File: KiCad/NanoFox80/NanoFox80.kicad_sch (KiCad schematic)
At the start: 50 parts, among them J101 Conn_01x02, J102 Conn_01x02, J109 Conn_01x02, J111 DB9 Female, J112 Conn_01x02, J113 Conn_01x02, J115 Conn_01x02, P101 ISP/PDI, Q101 BSS84W-7-F, Q102 BSS138W-7-F, SW101 SW_SPST, U102 LP2985-3.3, U105 AVR128DA28, X101 SIT1566AC TCO

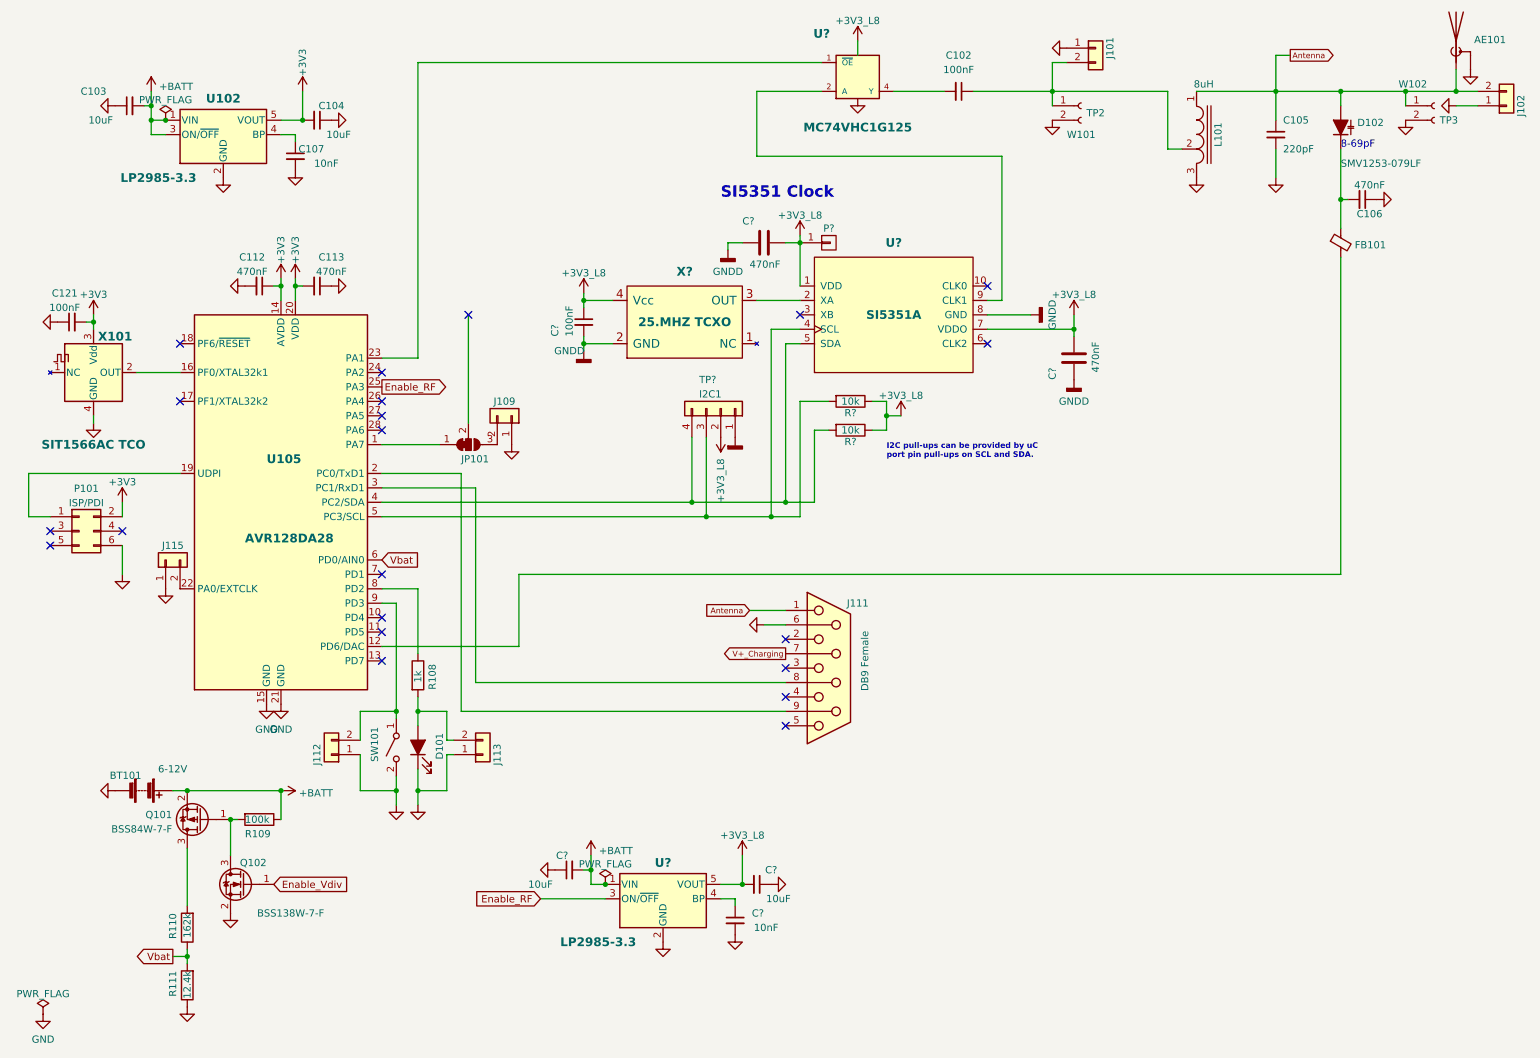
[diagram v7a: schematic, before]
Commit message: Development
o Addressed ERC errors
o Added trimmer capacitor
o Cosmetic changes to schematic
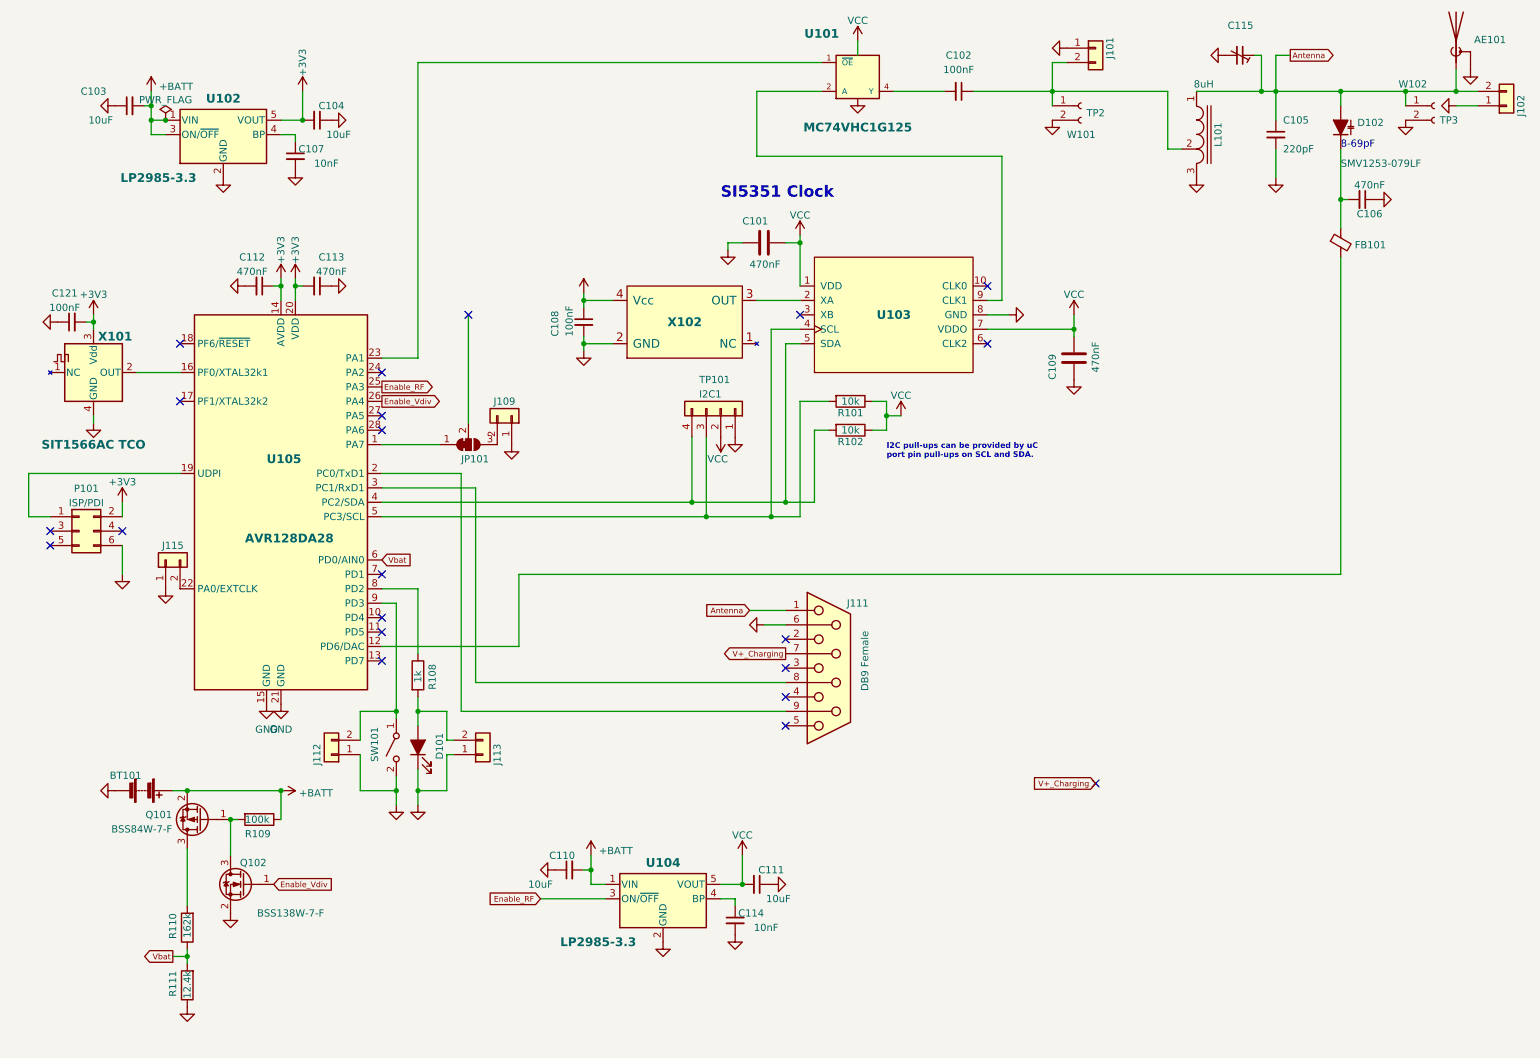
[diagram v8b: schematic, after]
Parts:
- removed P?: Thru, Pin_Headers:Pin_Header_Straight_1x01, symbol FlexFox80-rescue:CONN_01X01-ARDF-2-Band-MiniTx-rescue
- removed U?: SI5351A, Housings_SSOP:MSOP-10_3x3mm_Pitch0.5mm, symbol special:SI5351
- removed X?: 25.MHZ TCXO, Crystals:ASTX-H11-25.000MHZ, symbol special:ASTX-H11
- added C115: (no value), symbol Device:C_Trim_Small
- added U103: (no value), symbol Oscillator:SI5351
- added X102: (no value), symbol Oscillator:ASTX-H11
- BT101: value 6-12V -> (none)
- gave numbers to parts that had none: 11
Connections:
- net GNDD is gone; now on net GND: C101.2, C108.2, C109.2, TP101.1 (Pin_1)
- net Antenna: now also C115.1
- net Enable_Vdiv: now also U105.26 (PA4)
- net at R101.2, TP101.3 (Pin_3), U105.5 (PC3/SCL): now also U103.4 (SCL)
- net at R102.2, TP101.4 (Pin_4), U105.4 (PC2/SDA): now also U103.5 (SDA)
- net at U101.2 (A): now also U103.9 (CLK1)
- net +3V3_L8 renamed GND
- net GND: now also C115.2, U103.1 (VDD), U103.7 (VDDO), U103.8 (GND), X102.2 (GND), X102.4 (Vcc)
- new net: U103.2 (XA), X102.3 (OUT)
